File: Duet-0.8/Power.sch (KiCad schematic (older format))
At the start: 20 parts, among them U2 TC2117-3.3VDBTR, U3 MC7805CDTG

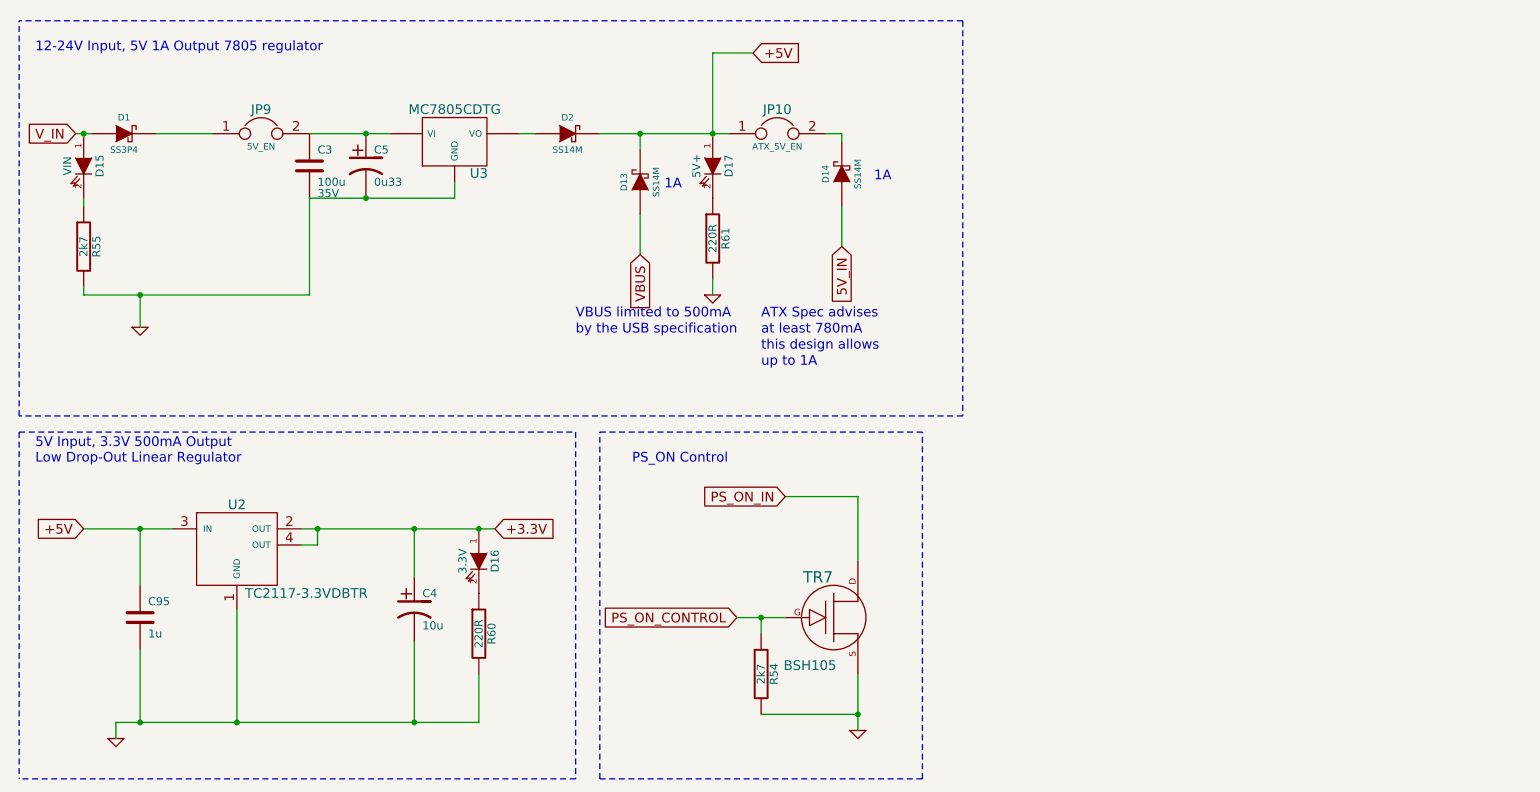
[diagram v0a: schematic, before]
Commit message: Duet Version 0.8 ----------------
Schematic changed; board still needs to be updated.

Changes:

Probe rewired to use AD12 and AD14, (standard P2 probe in the Firmware)
Bed connector - both spades and screw terminals used
Power connector - both spades and screw terminals used
Spurious power LEDS removed - there is now only one set
5V connector removed.  PS on is now a single pin.
Second Z connector added in series with the first.
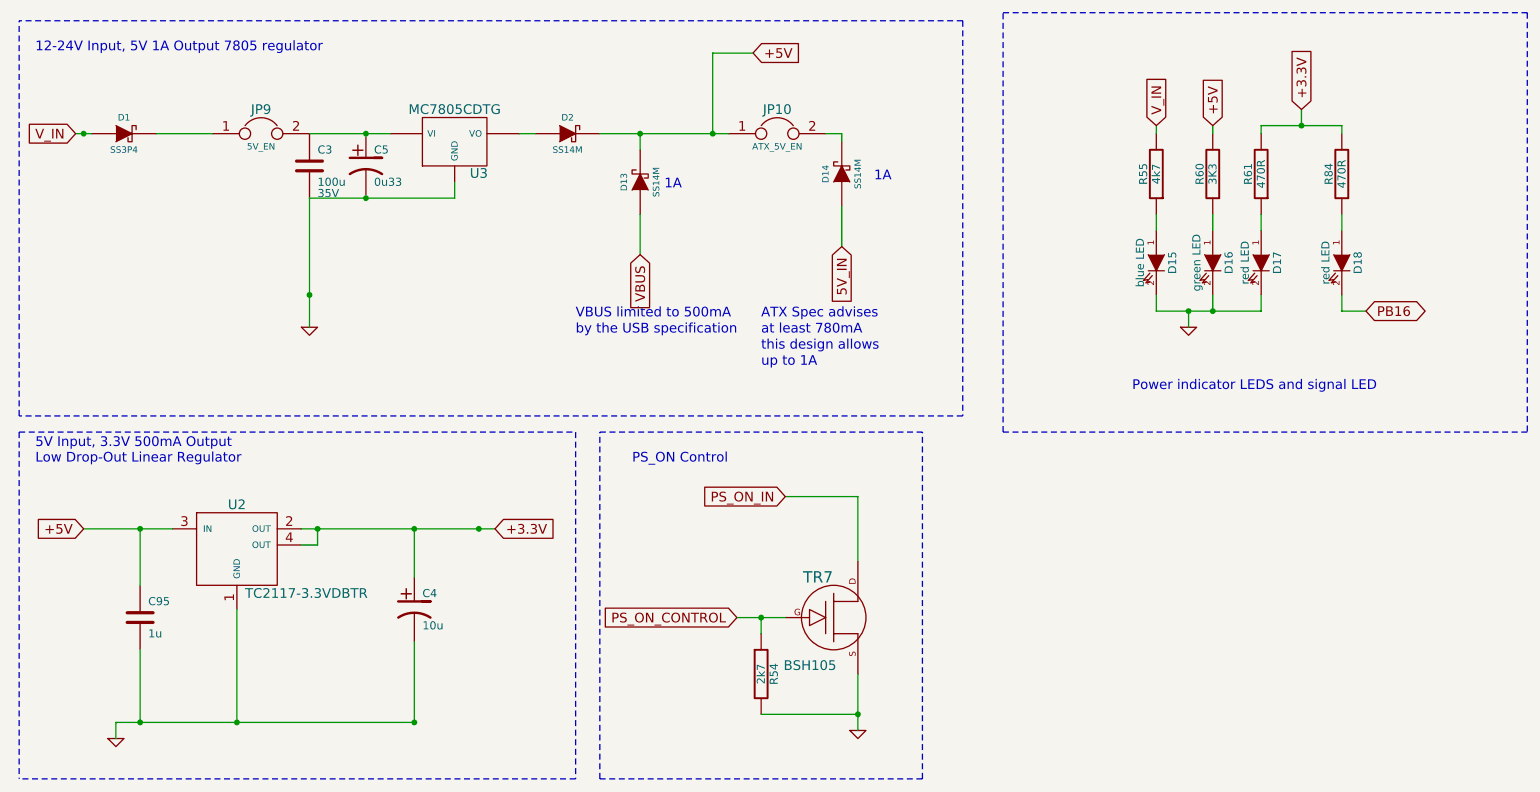
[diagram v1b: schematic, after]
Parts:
- added D18: red LED, symbol LED
- added R84: 470R, symbol R
- D15: value VIN -> blue LED
- D16: value 3.3V -> green LED
- D17: value 5V+ -> red LED
- R55: value 2k7 -> 4k7
- R60: value 220R -> 3K3
- R61: value 220R -> 470R
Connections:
- net +3.3V: now also R61.2, R84.2; no longer D16.1 (A)
- net +5V: now also R60.2; no longer D17.1 (A)
- net GND: now also D15.2 (K), D16.2 (K), D17.2 (K); no longer R55.2, R60.2, R61.2
- net V_IN: now also R55.2; no longer D15.1 (A)
- net at R55.1: now also D15.1 (A); no longer D15.2 (K)
- net at R61.1: now also D17.1 (A); no longer D17.2 (K)
- net at R60.1: now also D16.1 (A); no longer D16.2 (K)
- new net: D18.1 (A), R84.1
- new net PB16: D18.2 (K)
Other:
- note added: "Power indicator LEDS and signal LED"
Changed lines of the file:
@@
 LIBS:valves
 LIBS:FE
-LIBS:Duet0.7-cache
+LIBS:Shield-cache
+LIBS:Duet0.8-cache
 EELAYER 27 0
 EELAYER END
@@
 Sheet 3 7
 Title "Duet"
-Date "16 jan 2015"
+Date "27 feb 2015"
 Rev "0.7"
 Comp "Think3DPrint3D, RepRapPro"
@@
 Wire Wire Line
 	2150 4600 2150 4250
-Wire Wire Line
-	4250 5450 2000 5450
-Wire Wire Line
-	4250 5450 4250 5150
 Connection ~ 6000 4800
 Wire Wire Line
@@
 	5250 2550 5250 2300
 Wire Wire Line
-	2150 2800 2150 3000
+	3200 2200 3200 3000
 Wire Wire Line
 	6500 2500 6500 2250
@@
 	6000 5400 6600 5400
 Connection ~ 6600 5400
-Wire Wire Line
-	5700 2700 5700 2800
-Wire Wire Line
-	1800 2750 1800 2800
-Connection ~ 2150 2800
+Connection ~ 3200 2800
 Wire Wire Line
 	2150 5000 2150 5450
@@
 Connection ~ 4250 4250
 Wire Wire Line
-	1800 2250 1800 2200
-Wire Wire Line
 	1750 1800 1850 1800
 Connection ~ 1800 1800
 Wire Wire Line
-	1800 2800 3200 2800
-Wire Wire Line
-	3200 2800 3200 2200
-Wire Wire Line
-	3200 2200 4100 2200
+	4100 2200 3200 2200
 Connection ~ 3550 2200
 Wire Wire Line
@@
 	1    2150 4800
 	1    0    0    -1
-$EndComp
-$Comp
-L LED D16
-U 1 1 53B03C27
-P 4250 4450
-F 0 "D16" H 4250 4550 50  0000 C CNN
-F 1 "3.3V" H 4250 4350 50  0000 C CNN
-F 2 "" H 4250 4450 60  0001 C CNN
-F 3 "" H 4250 4450 60  0001 C CNN
-	1    4250 4450
-	0    1    1    0
-$EndComp
-$Comp
-L R R60
-U 1 1 53B03C26
-P 4250 4900
-F 0 "R60" V 4330 4900 50  0000 C CNN
-F 1 "220R" V 4250 4900 50  0000 C CNN
-F 2 "" H 4250 4900 60  0001 C CNN
-F 3 "" H 4250 4900 60  0001 C CNN
-	1    4250 4900
-	1    0    0    -1
-$EndComp
-$Comp
-L LED D17
-U 1 1 53B03C01
-P 5700 2000
-F 0 "D17" H 5700 2100 50  0000 C CNN
-F 1 "5V+" H 5700 1900 50  0000 C CNN
-F 2 "" H 5700 2000 60  0001 C CNN
-F 3 "" H 5700 2000 60  0001 C CNN
-	1    5700 2000
-	0    1    1    0
-$EndComp
-$Comp
-L R R61
-U 1 1 53B03C00
-P 5700 2450
-F 0 "R61" V 5780 2450 50  0000 C CNN
-F 1 "220R" V 5700 2450 50  0000 C CNN
-F 2 "" H 5700 2450 60  0001 C CNN
-F 3 "" H 5700 2450 60  0001 C CNN
-	1    5700 2450
-	1    0    0    -1
-$EndComp
-$Comp
-L GND #PWR030
-U 1 1 53B03BFF
-P 5700 2800
-F 0 "#PWR030" H 5700 2800 30  0001 C CNN
-F 1 "GND" H 5700 2730 30  0001 C CNN
-F 2 "" H 5700 2800 60  0001 C CNN
-F 3 "" H 5700 2800 60  0001 C CNN
-	1    5700 2800
-	1    0    0    -1
-$EndComp
-$Comp
-L R R55
-U 1 1 53B03BE9
-P 1800 2500
-F 0 "R55" V 1880 2500 50  0000 C CNN
-F 1 "2k7" V 1800 2500 50  0000 C CNN
-F 2 "" H 1800 2500 60  0001 C CNN
-F 3 "" H 1800 2500 60  0001 C CNN
-	1    1800 2500
-	1    0    0    -1
-$EndComp
-$Comp
-L LED D15
-U 1 1 53B03BD1
-P 1800 2000
-F 0 "D15" H 1800 2100 50  0000 C CNN
-F 1 "VIN" H 1800 1900 50  0000 C CNN
-F 2 "" H 1800 2000 60  0001 C CNN
-F 3 "" H 1800 2000 60  0001 C CNN
-	1    1800 2000
-	0    1    1    0
 $EndComp
 $Comp
@@
 PS_ON Control
 $Comp
-L GND #PWR031
+L GND #PWR030
 U 1 1 5220BA8F
 P 6600 5500
-F 0 "#PWR031" H 6600 5500 30  0001 C CNN
+F 0 "#PWR030" H 6600 5500 30  0001 C CNN
 F 1 "GND" H 6600 5430 30  0001 C CNN
 F 2 "" H 6600 5500 60  0001 C CNN
@@
 +5V
 $Comp
-L GND #PWR032
+L GND #PWR031
 U 1 1 50522574
 P 2000 5550
-F 0 "#PWR032" H 2000 5550 30  0001 C CNN
+F 0 "#PWR031" H 2000 5550 30  0001 C CNN
 F 1 "GND" H 2000 5480 30  0001 C CNN
 F 2 "" H 2000 5550 60  0001 C CNN
@@
 $EndComp
 $Comp
-L GND #PWR033
+L GND #PWR032
 U 1 1 50522566
-P 2150 3000
-F 0 "#PWR033" H 2150 3000 30  0001 C CNN
-F 1 "GND" H 2150 2930 30  0001 C CNN
-F 2 "" H 2150 3000 60  0001 C CNN
-F 3 "" H 2150 3000 60  0001 C CNN
-	1    2150 3000
+P 3200 3000
+F 0 "#PWR032" H 3200 3000 30  0001 C CNN
+F 1 "GND" H 3200 2930 30  0001 C CNN
+F 2 "" H 3200 3000 60  0001 C CNN
+F 3 "" H 3200 3000 60  0001 C CNN
+	1    3200 3000
 	1    0    0    -1
 $EndComp
@@
 	1    0    0    -1
 $EndComp
+Wire Wire Line
+	8450 2300 8450 2400
+Wire Wire Line
+	8450 1800 8450 1750
+Wire Wire Line
+	8450 2800 8450 2900
+$Comp
+L LED D15
+U 1 1 54EF3DE2
+P 8450 2600
+F 0 "D15" H 8450 2700 50  0000 C CNN
+F 1 "blue LED" H 8450 2500 50  0000 C CNN
+F 2 "" H 8450 2600 60  0001 C CNN
+F 3 "" H 8450 2600 60  0001 C CNN
+	1    8450 2600
+	0    1    1    0
+$EndComp
+$Comp
+L R R55
+U 1 1 54EF3DE8
+P 8450 2050
+F 0 "R55" V 8530 2050 50  0000 C CNN
+F 1 "4k7" V 8450 2050 50  0000 C CNN
+F 2 "" H 8450 2050 60  0001 C CNN
+F 3 "" H 8450 2050 60  0001 C CNN
+	1    8450 2050
+	-1   0    0    1
+$EndComp
+Wire Wire Line
+	8800 2300 8800 2400
+Wire Wire Line
+	8800 1800 8800 1750
+Wire Wire Line
+	8800 2800 8800 2900
+$Comp
+L LED D16
+U 1 1 54EF3DF1
+P 8800 2600
+F 0 "D16" H 8800 2700 50  0000 C CNN
+F 1 "green LED" H 8800 2500 50  0000 C CNN
+F 2 "" H 8800 2600 60  0001 C CNN
+F 3 "" H 8800 2600 60  0001 C CNN
+	1    8800 2600
+	0    1    1    0
+$EndComp
+$Comp
+L R R60
+U 1 1 54EF3DF7
+P 8800 2050
+F 0 "R60" V 8880 2050 50  0000 C CNN
+F 1 "3K3" V 8800 2050 50  0000 C CNN
+F 2 "" H 8800 2050 60  0001 C CNN
+F 3 "" H 8800 2050 60  0001 C CNN
+	1    8800 2050
+	-1   0    0    1
+$EndComp
+Wire Wire Line
+	9100 2300 9100 2400
+Wire Wire Line
+	9100 1800 9100 1750
+Wire Wire Line
+	9100 2900 9100 2800
+$Comp
+L LED D17
+U 1 1 54EF3E00
+P 9100 2600
+F 0 "D17" H 9100 2700 50  0000 C CNN
+F 1 "red LED" H 9100 2500 50  0000 C CNN
+F 2 "" H 9100 2600 60  0001 C CNN
+F 3 "" H 9100 2600 60  0001 C CNN
+	1    9100 2600
+	0    1    1    0
+$EndComp
+$Comp
+L R R61
+U 1 1 54EF3E06
+P 9100 2050
+F 0 "R61" V 9180 2050 50  0000 C CNN
+F 1 "470R" V 9100 2050 50  0000 C CNN
+F 2 "" H 9100 2050 60  0001 C CNN
+F 3 "" H 9100 2050 60  0001 C CNN
+	1    9100 2050
+	-1   0    0    1
+$EndComp
+Wire Wire Line
+	9600 2300 9600 2400
+Wire Wire Line
+	9600 1800 9600 1750
+Wire Wire Line
+	9600 2800 9600 2900
+$Comp
+L LED D18
+U 1 1 54EF3E0F
+P 9600 2600
+F 0 "D18" H 9600 2700 50  0000 C CNN
+F 1 "red LED" H 9600 2500 50  0000 C CNN
+F 2 "" H 9600 2600 60  0001 C CNN
+F 3 "" H 9600 2600 60  0001 C CNN
+	1    9600 2600
+	0    1    1    0
+$EndComp
+$Comp
+L R R84
+U 1 1 54EF3E15
+P 9600 2050
+F 0 "R84" V 9680 2050 50  0000 C CNN
+F 1 "470R" V 9600 2050 50  0000 C CNN
+F 2 "" H 9600 2050 60  0001 C CNN
+F 3 "" H 9600 2050 60  0001 C CNN
+	1    9600 2050
+	-1   0    0    1
+$EndComp
+Wire Wire Line
+	8450 2900 9100 2900
+Connection ~ 8800 2900
+Wire Wire Line
+	8650 2900 8650 3000
+Connection ~ 8650 2900
+Wire Wire Line
+	9600 1750 9100 1750
+Wire Wire Line
+	9350 1750 9350 1650
+Connection ~ 9350 1750
+Text GLabel 8450 1750 1    60   Input ~ 0
+V_IN
+Text GLabel 8800 1750 1    60   Input ~ 0
++5V
+Text GLabel 9350 1650 1    60   Input ~ 0
++3.3V
+$Comp
+L GND #PWR033
+U 1 1 54EF3E25
+P 8650 3000
+F 0 "#PWR033" H 8650 3000 30  0001 C CNN
+F 1 "GND" H 8650 2930 30  0001 C CNN
+F 2 "" H 8650 3000 60  0001 C CNN
+F 3 "" H 8650 3000 60  0001 C CNN
+	1    8650 3000
+	1    0    0    -1
+$EndComp
+Text GLabel 9750 2900 2    60   BiDi ~ 0
+PB16
+Wire Wire Line
+	9600 2900 9750 2900
+Wire Notes Line
+	7500 1050 10750 1050
+Wire Notes Line
+	10750 1050 10750 3650
+Wire Notes Line
+	10750 3650 7500 3650
+Wire Notes Line
+	7500 3650 7500 1050
+Text Notes 8300 3400 0    60   ~ 0
+Power indicator LEDS and signal LED
+Wire Wire Line
+	2000 5450 3850 5450
 $EndSCHEMATC

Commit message: Board half done...
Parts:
- removed D14: SS14M, symbol DIODESCH
- removed JP10: ATX_5V_EN, symbol JUMPER
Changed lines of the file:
@@
 Connection ~ 5250 1800
 Wire Wire Line
-	5250 1900 5250 1800
+	5250 1800 5250 1900
 Wire Wire Line
 	4100 2100 4100 2200
@@
 Wire Notes Line
 	5000 3650 7000 3650
-Wire Wire Line
-	6400 1800 6500 1800
 Wire Wire Line
 	5950 1300 5700 1300
@@
 Wire Wire Line
 	3200 2200 3200 3000
-Wire Wire Line
-	6500 2500 6500 2250
-Wire Wire Line
-	6500 1800 6500 1850
-Wire Wire Line
-	5000 1800 5800 1800
 Wire Wire Line
 	6600 5500 6600 5150
@@
 	1    0    0    -1
 $EndComp
-Text Notes 6700 2100 0    60   ~ 0
-1A
-$Comp
-L DIODESCH D14
-U 1 1 5220D356
-P 6500 2050
-F 0 "D14" H 6500 2150 40  0000 C CNN
-F 1 "SS14M" H 6500 1950 40  0000 C CNN
-F 2 "" H 6500 2050 60  0001 C CNN
-F 3 "" H 6500 2050 60  0001 C CNN
-	1    6500 2050
-	0    -1   -1   0
-$EndComp
 $Comp
 L BSH105 TR7
@@
 Text GLabel 6150 4050 0    60   Input ~ 0
 PS_ON_IN
-$Comp
-L JUMPER JP10
-U 1 1 5220B966
-P 6100 1800
-F 0 "JP10" H 6100 1950 60  0000 C CNN
-F 1 "ATX_5V_EN" H 6100 1720 40  0000 C CNN
-F 2 "" H 6100 1800 60  0001 C CNN
-F 3 "" H 6100 1800 60  0001 C CNN
-	1    6100 1800
-	1    0    0    -1
-$EndComp
 Text Notes 5400 2150 0    60   ~ 0
 1A
@@
 Text Notes 6000 2950 0    60   ~ 0
 ATX Spec advises
-Text GLabel 6500 2500 3    60   Input ~ 0
-5V_IN
 Text Notes 4850 3050 0    60   ~ 0
 by the USB specification
@@
 Wire Wire Line
 	2000 5450 3850 5450
+Wire Wire Line
+	5700 1800 5000 1800
 $EndSCHEMATC
